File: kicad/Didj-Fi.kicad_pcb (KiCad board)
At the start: 2 copper layers, 44.9 x 33.5 mm, 20 parts, among them J1 didj_cart, J3 USB_B_Micro, U1 CH340E, U2 ESP-12F

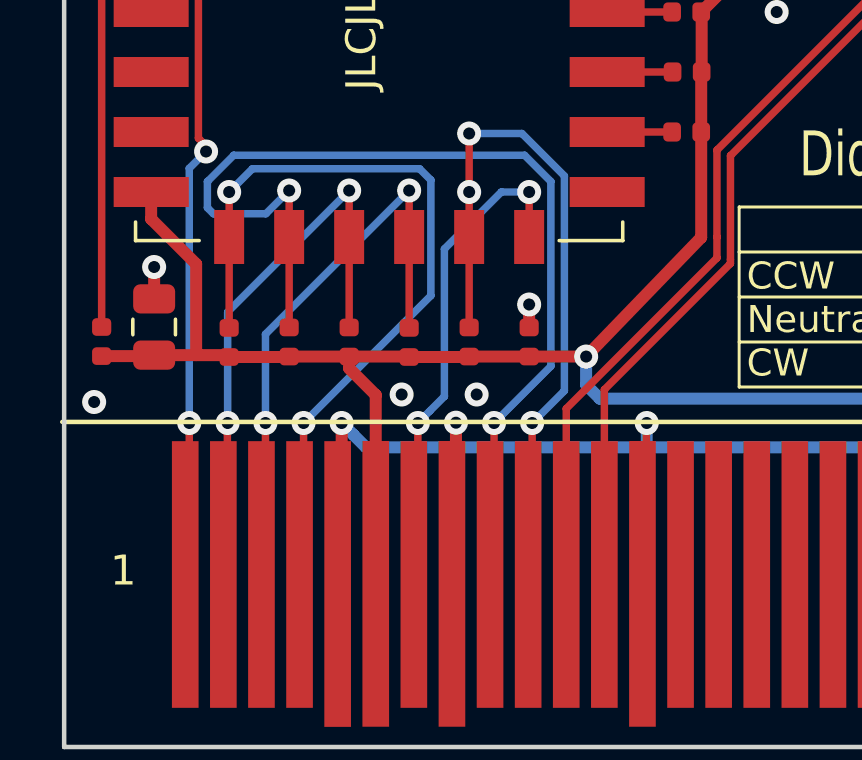
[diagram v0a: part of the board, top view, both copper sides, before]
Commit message: minor tweaks
removed an extra via
re-routed a couple of traces
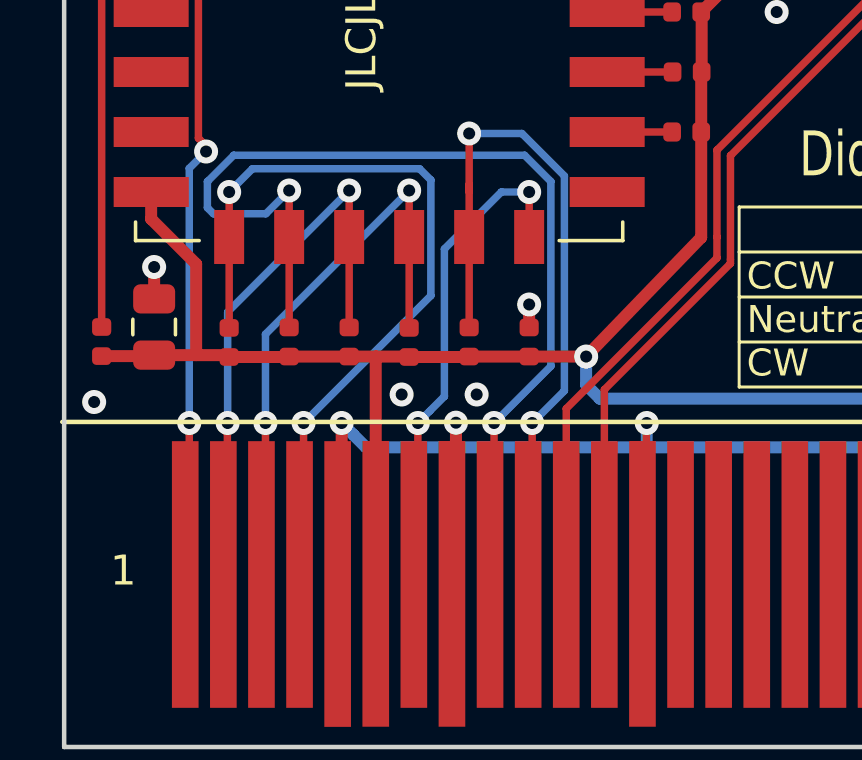
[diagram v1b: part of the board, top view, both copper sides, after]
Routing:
- net /DAT1: vias 3 -> 2
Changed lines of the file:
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@@
     (thickness 1.6)
     (drawings 23)
-    (tracks 234)
+    (tracks 233)
     (zones 0)
     (modules 20)
@@
   (segment (start 125.6 111.105) (end 127.6 111.105) (width 0.4) (layer F.Cu) (net 1))
   (segment (start 129.585 111.105) (end 129.6 111.12) (width 0.4) (layer F.Cu) (net 1))
-  (segment (start 127.6 111.105) (end 129.585 111.105) (width 0.4) (layer F.Cu) (net 1))
   (segment (start 131.585 111.12) (end 131.6 111.105) (width 0.4) (layer F.Cu) (net 1))
   (segment (start 129.6 111.12) (end 131.585 111.12) (width 0.4) (layer F.Cu) (net 1))
@@
   (via (at 135.50001 111.105) (size 0.8) (drill 0.4) (layers F.Cu B.Cu) (net 1))
   (segment (start 135.50001 111.105) (end 139.335 107.135) (width 0.4) (layer F.Cu) (net 1))
-  (segment (start 128.4865 112.3865) (end 128.4865 118.3695) (width 0.4) (layer F.Cu) (net 1))
-  (segment (start 127.6 111.5) (end 128.4865 112.3865) (width 0.4) (layer F.Cu) (net 1))
-  (segment (start 127.6 111.105) (end 127.6 111.5) (width 0.4) (layer F.Cu) (net 1))
   (segment (start 122.5 108.02) (end 122.5 111.0575) (width 0.4) (layer F.Cu) (net 1))
   (segment (start 121 105.62) (end 121 106.52) (width 0.4) (layer F.Cu) (net 1))
@@
   (segment (start 121 106.52) (end 122.5 108.02) (width 0.4) (layer F.Cu) (net 1))
   (segment (start 122.5 111.0575) (end 123.5375 111.0575) (width 0.4) (layer F.Cu) (net 1))
+  (segment (start 128.4865 118.3695) (end 128.4865 111.1185) (width 0.4) (layer F.Cu) (net 1))
+  (segment (start 127.6 111.105) (end 128.5 111.105) (width 0.4) (layer F.Cu) (net 1))
+  (segment (start 128.4865 111.1185) (end 128.5 111.105) (width 0.4) (layer F.Cu) (net 1))
+  (segment (start 128.5 111.105) (end 129.585 111.105) (width 0.4) (layer F.Cu) (net 1))
   (via (at 121.1 108.12) (size 0.8) (drill 0.4) (layers F.Cu B.Cu) (net 2))
   (segment (start 121.1 109.1825) (end 121.1 108.12) (width 0.4) (layer F.Cu) (net 2))
@@
   (segment (start 133.7 118.3695) (end 133.7 113.32) (width 0.25) (layer F.Cu) (net 3))
   (segment (start 131.6 110.135) (end 131.6 107.12) (width 0.25) (layer F.Cu) (net 3))
-  (via (at 131.6 105.62) (size 0.8) (drill 0.4) (layers F.Cu B.Cu) (net 3))
   (segment (start 131.6 105.37) (end 131.6 107.12) (width 0.25) (layer F.Cu) (net 3))
   (segment (start 133.359401 103.669989) (end 131.6 103.669989) (width 0.25) (layer B.Cu) (net 3))

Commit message: silk screen changes
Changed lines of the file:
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@@
     (fp_line (start 0 0) (end 0 10.8) (layer Dwgs.User) (width 0.15))
     (fp_line (start 0 0) (end 45 0) (layer F.SilkS) (width 0.15))
-    (fp_text user 1 (at 2.032 4.958) (layer F.SilkS)
-      (effects (font (size 1 1) (thickness 0.15)))
-    )
-    (fp_text user 30 (at 42.926 4.958) (layer F.SilkS)
+    (fp_text user 1 (at 2.032 4.958) (layer F.SilkS) hide
+      (effects (font (size 1 1) (thickness 0.15)))
+    )
+    (fp_text user 30 (at 42.926 4.958) (layer F.SilkS) hide
       (effects (font (size 1 1) (thickness 0.15)))
     )
@@
     (effects (font (size 0.9 0.9) (thickness 0.15)) (justify left))
   )
-  (gr_text "Didj-Fi v1.0" (at 139.35 92.87) (layer B.SilkS)
-    (effects (font (size 2 2) (thickness 0.4)) (justify left mirror))
+  (gr_text "Didj-Fi v1.0" (at 133.25 92.5) (layer B.SilkS)
+    (effects (font (size 1.5 1.5) (thickness 0.3)) (justify left mirror))
   )
   (gr_text JLCJLCJLCJLC (at 128.006 97.986 90) (layer F.SilkS)
     (effects (font (size 1 1) (thickness 0.15)))
   )
-  (gr_text jkent.net/w/didjfi (at 136.35 95.62) (layer B.SilkS)
-    (effects (font (size 1.5 0.9) (thickness 0.15)) (justify left mirror))
+  (gr_text jkent.net/w/didjfi (at 132.75 95.25) (layer B.SilkS)
+    (effects (font (size 1.5 1) (thickness 0.15)) (justify left mirror))
   )
   (gr_text "Didj-Fi v1.0" (at 142.6 104.37) (layer F.SilkS)

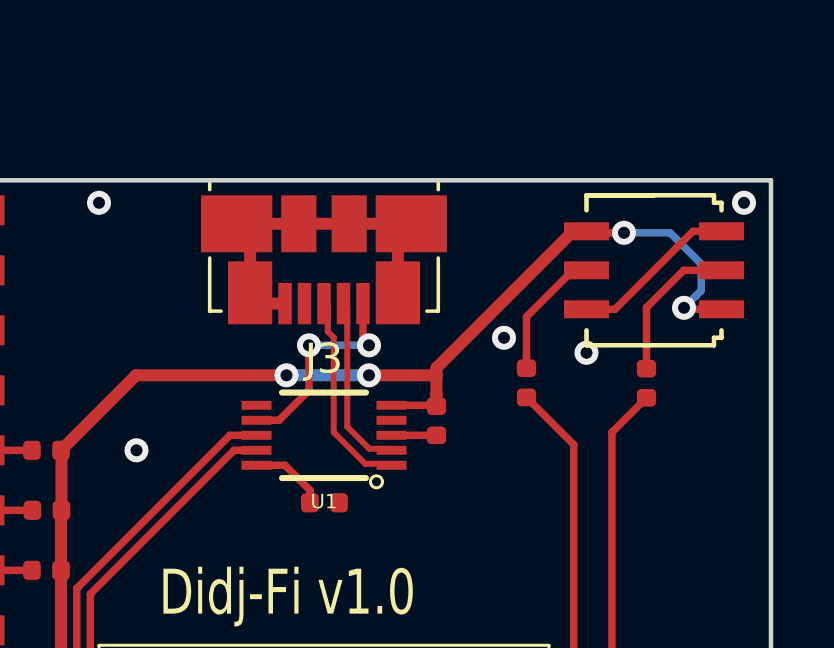
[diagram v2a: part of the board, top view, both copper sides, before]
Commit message: change usb footprint
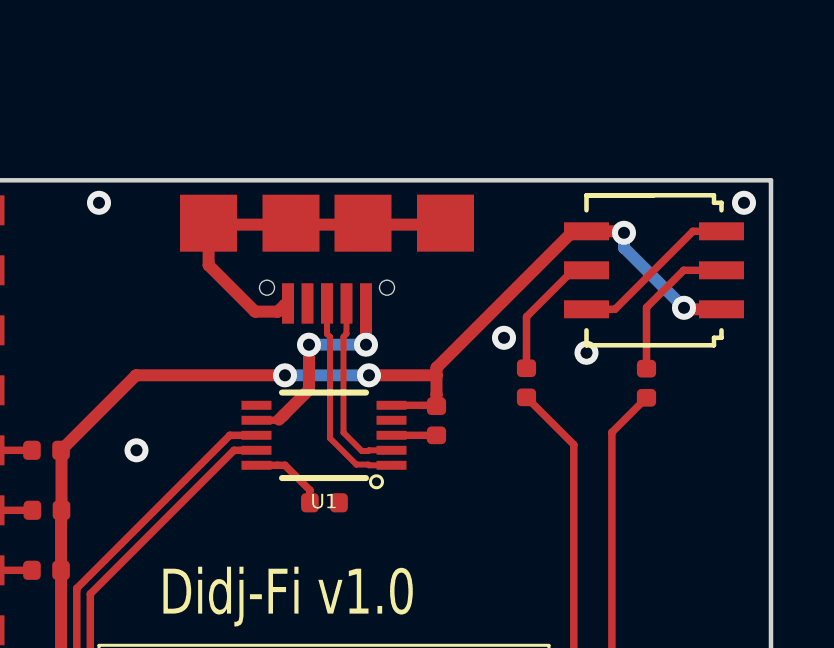
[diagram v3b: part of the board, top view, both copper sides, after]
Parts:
- J3: footprint Connector_USB:USB_Micro-B_Molex_47346-0001 -> project:C40942
- moved J3 1.22 mm to (148.2, 92.0), turned to 0 degrees
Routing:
- net +3V3: track 94.5 -> 93.2 mm
- net GND: track 65.2 -> 65.7 mm
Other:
- net class Power: trace_width 0.4 -> 0.25

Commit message: prepare for manufacture
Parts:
- turned U1 to 90 degrees
